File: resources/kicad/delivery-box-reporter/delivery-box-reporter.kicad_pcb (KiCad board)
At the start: 2 copper layers, 40 x 60.5 mm, 11 parts, among them J1 Solar Panel, Q2 2N3904, U1 ESP8266 D1 Mini, U4 TLV803EB33VDBZR, U5 MCP1702-3302E

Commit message: Updated PCB
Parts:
- added U3: ~, Sensor_Distance:GY-VL53LOX-V2, B.Cu at (142.8, 128.0)
- J1: moved to B.Cu
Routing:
- net unconnected-(U3-GPIO1-Pad5): track 0.00 -> 8.50 mm
- net Net-(U1-MISO/D6): track 44.6 -> 53.1 mm
- net Net-(DISP1-SDA): track 67.4 -> 75.9 mm
- net Net-(DISP1-SCL): track 82.6 -> 90.9 mm
- net +3.3V: track 94.5 -> 102.2 mm
- net Earth: track 105.8 -> 113.2 mm
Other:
- board size 40 x 60.5 mm -> 40 x 60 mm
- board text added: "+"
- board text added: "+3v3-"
- board text added: "-"
- board text added: "Delivery Box Reporter Version 1.2.1 12-11-24 David E. Powell"
- board text removed: "Delivery Box Reporter Version 1.0 12-2-24 David E. Powell"

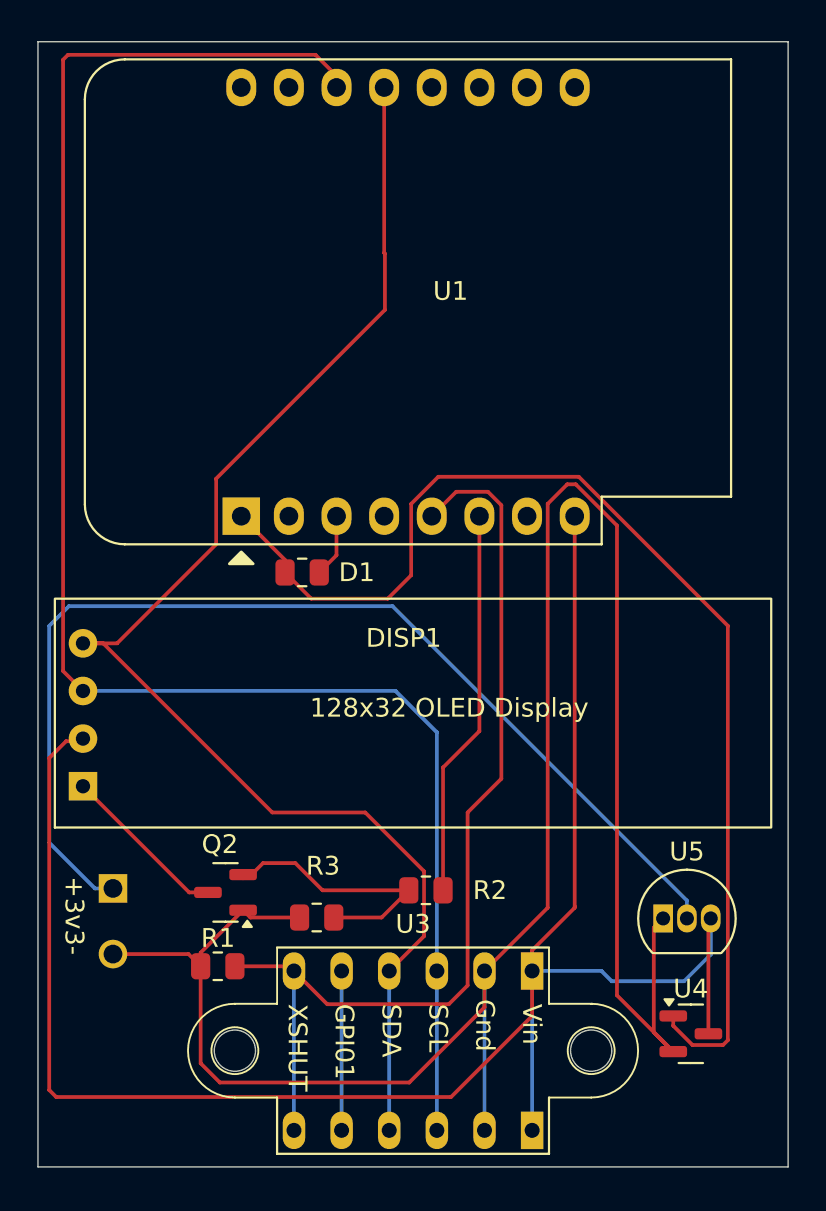
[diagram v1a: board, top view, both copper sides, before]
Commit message: Changes to board and minor code changes.
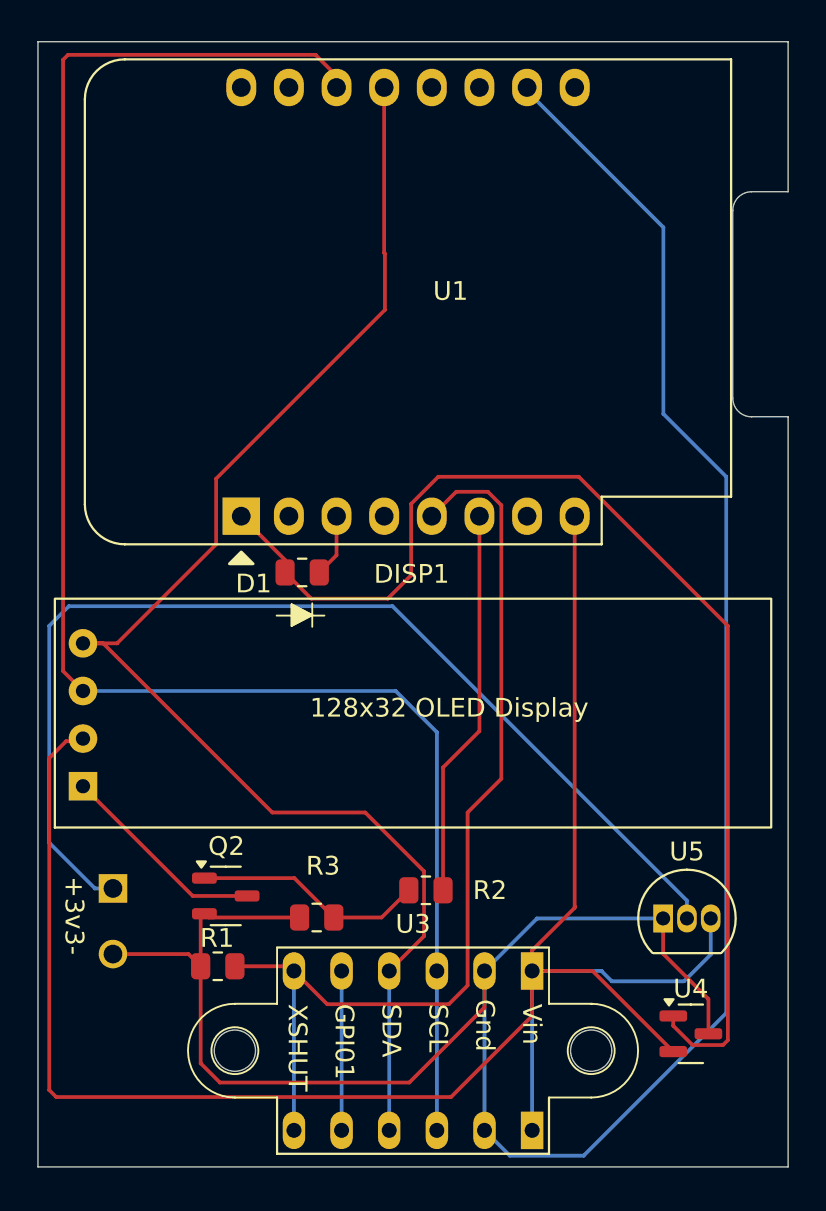
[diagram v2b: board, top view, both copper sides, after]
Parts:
- Q2: footprint Package_TO_SOT_SMD:SOT-23 -> Davids_Footprints:MMBT3904-7-F_SOT-23-3
- moved Q2 0.19 mm to (132.8, 115.5), turned to 0 degrees
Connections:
- Q2 pad 1: Earth -> Net-(Q2-B)
- Q2 pad 2: Net-(Q2-B) -> Earth
- U1 pad 10: unconnected-(U1-GND-Pad10) -> Earth
- U4 pad 2: Earth -> +3.3V
- U4 pad 3: +3.3V -> Earth
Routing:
- net Earth: track 113.2 -> 134.0 mm
- net +3.3V: track 102.2 -> 105.5 mm
- net Net-(DISP1-Gnd): track 9.01 -> 11.2 mm
- net Net-(Q2-B): track 14.5 -> 12.4 mm
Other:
- outline, holes or cut-outs redrawn
- board text added: "Delivery Box Reporter Version 1.4.0 12-17-24 David E. Powell"
- board text removed: "Delivery Box Reporter Version 1.2.1 12-11-24 David E. Powell"
